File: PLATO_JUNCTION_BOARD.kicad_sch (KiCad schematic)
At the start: 28 parts, among them J1 DE9_Receptacle_MountingHoles, J2 TFM-108-02-L-D, J3 TFM-108-02-L-D, U1 R-78E5.0-0.5

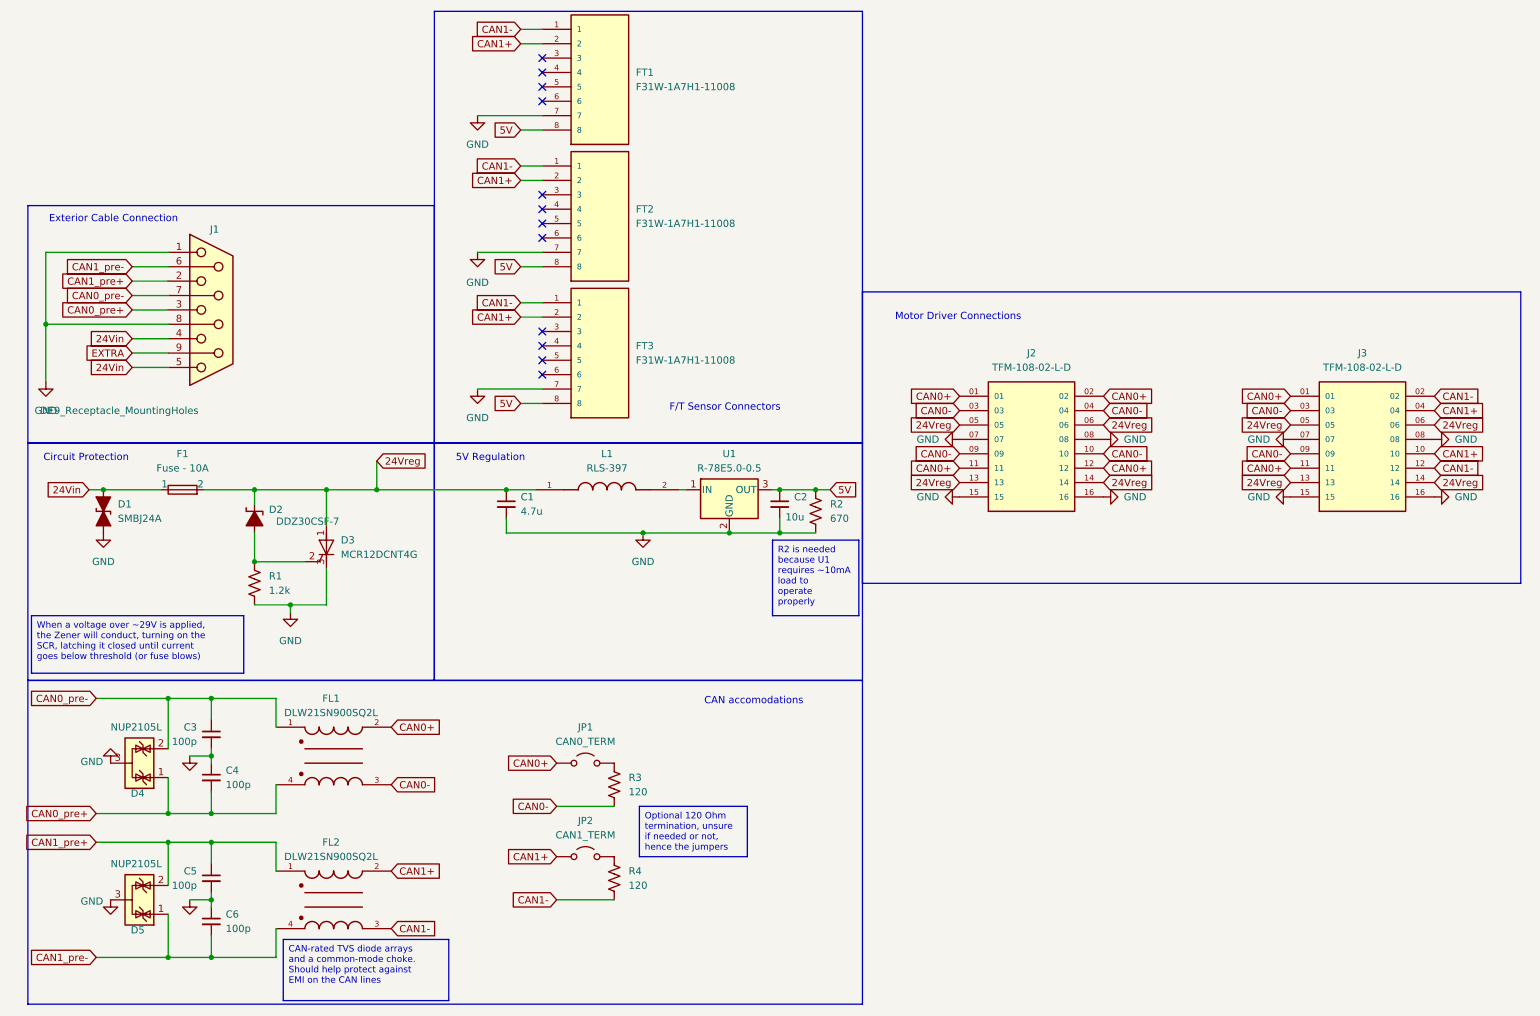
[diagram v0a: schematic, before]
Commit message: Removed choke, added new connector
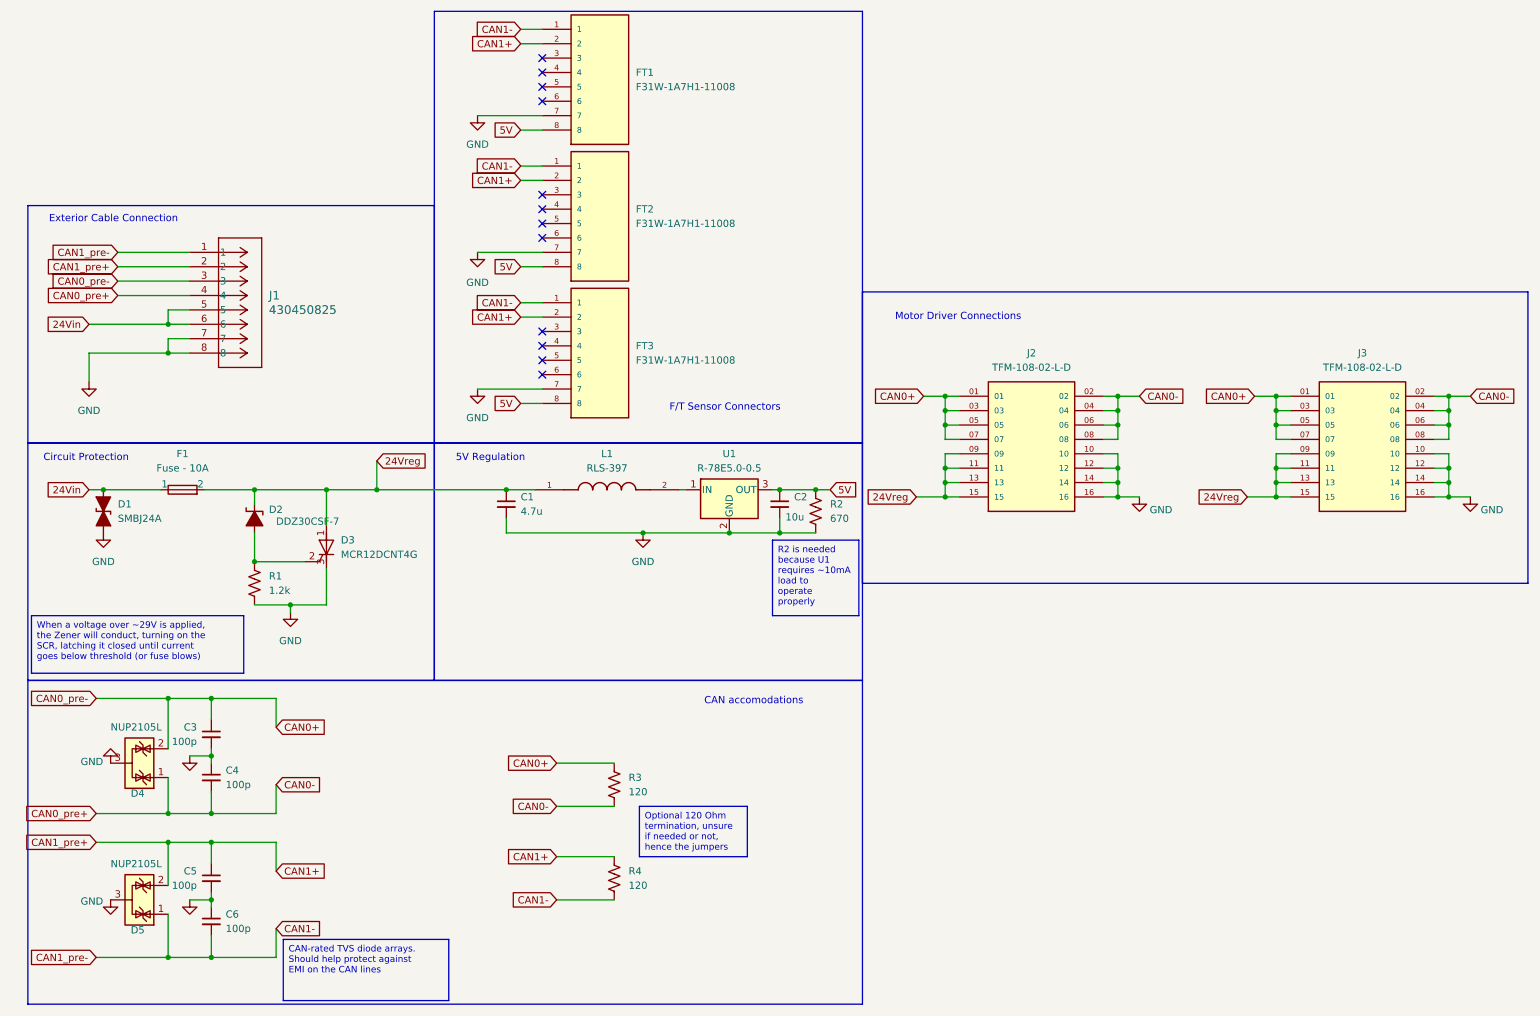
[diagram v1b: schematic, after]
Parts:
- removed FL1, FL2: DLW21SN900SQ2L, DLW21SN900SQ2L:DLW21SN900SQ2L, symbol DLW21SN900SQ2L:DLW21SN900SQ2L
- removed J1: DE9_Receptacle_MountingHoles, Connector_Dsub:DSUB-9_Female_Horizontal_P2.77x2.54mm_EdgePinOffset9.40mm, symbol Connector:DE9_Receptacle
- removed JP1: CAN0_TERM, JumperVariant:SolderJumper-2_P1.3mm_Open_Pad1.0x1.5mm_SMALLER, symbol Jumper:Jumper_2_Open
- removed JP2: CAN1_TERM, JumperVariant:SolderJumper-2_P1.3mm_Open_Pad1.0x1.5mm_SMALLER, symbol Jumper:Jumper_2_Open
- added J1: 430450825, 0430450825:0430450825, symbol 0430450825:430450825
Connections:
- net CAN0_pre+ is gone; now on net CAN0-: C4.2, D4.1 (K)
- net CAN0_pre- is gone; now on net CAN0+: C3.1, D4.2 (K)
- net CAN1_pre+ is gone; now on net CAN1+: C5.1, D5.2 (K)
- net CAN1_pre- is gone; now on net CAN1-: C6.2, D5.1 (K)
- net 24Vin: now also J1.5, J1.6
- net 24Vreg: now also J2.09, J2.11, J2.15, J3.09, J3.11, J3.15; no longer J2.05, J2.06, J2.14, J3.05, J3.06, J3.14
- net CAN0+: now also J2.03, J2.05, J2.07, J3.03, J3.05, J3.07, R3.1, J1.3; no longer J2.02, J2.11, J2.12, J3.11
- net CAN0-: now also J2.02, J2.06, J2.08, J3.02, J3.04, J3.06, J3.08, J1.4; no longer J2.03, J2.09, J2.10, J3.03, J3.09
- net CAN1+: now also R4.1, J1.2; no longer J3.04, J3.10
- net CAN1-: now also J1.1; no longer J3.02, J3.12
- net GND: now also J2.10, J2.12, J2.14, J3.10, J3.12, J3.14, J1.7, J1.8; no longer J2.07, J2.08, J2.15, J3.07, J3.08, J3.15

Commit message: moved 24V and GND pins on J1, changed GND pads to square shapes
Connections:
- net 24Vin: now also J1.7; no longer J1.5
- net GND: now also J1.10, J1.5, J1.9; no longer J1.7
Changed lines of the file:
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@@
 	)
 	(junction
-		(at 102.87 106.68)
+		(at 21.59 82.55)
 		(diameter 0)
 		(color 0 0 0 0)
 	)
 	(junction
-		(at 43.18 82.55)
+		(at 102.87 106.68)
 		(diameter 0)
 		(color 0 0 0 0)
@@
 	)
 	(junction
-		(at 43.18 77.47)
-		(diameter 0)
-		(color 0 0 0 0)
-	)
-	(junction
 		(at 210.82 92.71)
 		(diameter 0)
@@
 	)
 	(junction
+		(at 45.72 77.47)
+		(diameter 0)
+		(color 0 0 0 0)
+	)
+	(junction
 		(at 238.76 95.25)
 		(diameter 0)
@@
 	(wire
 		(pts
-			(xy 29.21 77.47) (xy 43.18 77.47)
-		)
-		(stroke
-			(width 0)
-			(type default)
-		)
-	)
-	(wire
-		(pts
 			(xy 102.87 114.3) (xy 127 114.3)
 		)
@@
 	(wire
 		(pts
+			(xy 45.72 77.47) (xy 45.72 80.01)
+		)
+		(stroke
+			(width 0)
+			(type default)
+		)
+	)
+	(wire
+		(pts
 			(xy 97.79 40.64) (xy 109.22 40.64)
 		)
@@
 	(wire
 		(pts
+			(xy 62.23 59.69) (xy 55.88 59.69)
+		)
+		(stroke
+			(width 0)
+			(type default)
+		)
+	)
+	(wire
+		(pts
 			(xy 273.05 107.95) (xy 269.24 107.95)
 		)
@@
 	(wire
 		(pts
-			(xy 43.18 80.01) (xy 46.99 80.01)
-		)
-		(stroke
-			(width 0)
-			(type default)
-		)
-	)
-	(wire
-		(pts
 			(xy 273.05 90.17) (xy 269.24 90.17)
 		)
@@
 	(wire
 		(pts
-			(xy 29.21 82.55) (xy 43.18 82.55)
-		)
-		(stroke
-			(width 0)
-			(type default)
-		)
-	)
-	(wire
-		(pts
 			(xy 238.76 102.87) (xy 241.3 102.87)
 		)
@@
 	(wire
 		(pts
-			(xy 43.18 77.47) (xy 43.18 74.93)
-		)
-		(stroke
-			(width 0)
-			(type default)
-		)
-	)
-	(wire
-		(pts
 			(xy 214.63 90.17) (xy 210.82 90.17)
 		)
@@
 	(wire
 		(pts
-			(xy 43.18 74.93) (xy 46.99 74.93)
-		)
-		(stroke
-			(width 0)
-			(type default)
-		)
-	)
-	(wire
-		(pts
 			(xy 105.41 43.18) (xy 109.22 43.18)
 		)
@@
 	(wire
 		(pts
-			(xy 43.18 77.47) (xy 46.99 77.47)
-		)
-		(stroke
-			(width 0)
-			(type default)
-		)
-	)
-	(wire
-		(pts
 			(xy 43.18 189.23) (xy 50.8 189.23)
 		)
@@
 	(wire
 		(pts
-			(xy 43.18 82.55) (xy 46.99 82.55)
+			(xy 105.41 52.07) (xy 109.22 52.07)
 		)
 		(stroke
@@
 	(wire
 		(pts
-			(xy 105.41 52.07) (xy 109.22 52.07)
+			(xy 45.72 80.01) (xy 46.99 80.01)
 		)
 		(stroke
@@
 	(wire
 		(pts
-			(xy 29.21 82.55) (xy 29.21 87.63)
+			(xy 21.59 82.55) (xy 21.59 83.82)
 		)
 		(stroke
@@
 	(wire
 		(pts
+			(xy 46.99 74.93) (xy 21.59 74.93)
+		)
+		(stroke
+			(width 0)
+			(type default)
+		)
+	)
+	(wire
+		(pts
 			(xy 50.8 160.02) (xy 50.8 163.83)
 		)
@@
 	(wire
 		(pts
+			(xy 34.29 77.47) (xy 45.72 77.47)
+		)
+		(stroke
+			(width 0)
+			(type default)
+		)
+	)
+	(wire
+		(pts
 			(xy 176.53 90.17) (xy 180.34 90.17)
 		)
@@
 	(wire
 		(pts
-			(xy 43.18 80.01) (xy 43.18 82.55)
+			(xy 21.59 74.93) (xy 21.59 82.55)
 		)
 		(stroke
@@
 	(wire
 		(pts
+			(xy 45.72 77.47) (xy 46.99 77.47)
+		)
+		(stroke
+			(width 0)
+			(type default)
+		)
+	)
+	(wire
+		(pts
 			(xy 157.48 106.68) (xy 160.02 106.68)
 		)
@@
 	(wire
 		(pts
+			(xy 21.59 82.55) (xy 46.99 82.55)
+		)
+		(stroke
+			(width 0)
+			(type default)
+		)
+	)
+	(wire
+		(pts
 			(xy 43.18 168.91) (xy 43.18 176.53)
 		)
@@
 	(global_label "24Vin"
 		(shape input)
-		(at 29.21 77.47 180)
+		(at 34.29 77.47 180)
 		(fields_autoplaced yes)
 		(effects
@@
 		)
 		(property "Intersheetrefs" "${INTERSHEET_REFS}"
-			(at 20.9634 77.47 0)
+			(at 26.0434 77.47 0)
 			(effects
 				(font
@@
 		(pin "4"
 		)
+		(pin "9"
+		)
+		(pin "10"
+		)
 		(instances
 			(project ""
@@
 	)
 	(symbol
+		(lib_id "power:GND")
+		(at 62.23 59.69 0)
+		(mirror y)
+		(unit 1)
+		(exclude_from_sim no)
+		(in_bom yes)
+		(on_board yes)
+		(dnp no)
+		(fields_autoplaced yes)
+		(property "Reference" "#PWR10"
+			(at 62.23 66.04 0)
+			(effects
+				(font
+					(size 1.27 1.27)
+				)
+				(hide yes)
+			)
+		)
+		(property "Value" "GND"
+			(at 62.2301 63.5 90)
+			(effects
+				(font
+					(size 1.27 1.27)
+				)
+				(justify right)
+				(hide yes)
+			)
+		)
+		(property "Footprint" ""
+			(at 62.23 59.69 0)
+			(effects
+				(font
+					(size 1.27 1.27)
+				)
+				(hide yes)
+			)
+		)
+		(property "Datasheet" ""
+			(at 62.23 59.69 0)
+			(effects
+				(font
+					(size 1.27 1.27)
+				)
+				(hide yes)
+			)
+		)
+		(property "Description" "Power symbol creates a global label with name \"GND\" , ground"
+			(at 62.23 59.69 0)
+			(effects
+				(font
+					(size 1.27 1.27)
+				)
+				(hide yes)
+			)
+		)
+		(pin "1"
+		)
+		(instances
+			(project "PLATO_JUNCTION_BOARD"
+				(path "/b029bc8a-eb1a-4550-a6f9-ce3f11ff00d6"
+					(reference "#PWR10")
+					(unit 1)
+				)
+			)
+		)
+	)
+	(symbol
+		(lib_id "power:GND")
+		(at 55.88 87.63 0)
+		(mirror y)
+		(unit 1)
+		(exclude_from_sim no)
+		(in_bom yes)
+		(on_board yes)
+		(dnp no)
+		(fields_autoplaced yes)
+		(property "Reference" "#PWR9"
+			(at 55.88 93.98 0)
+			(effects
+				(font
+					(size 1.27 1.27)
+				)
+				(hide yes)
+			)
+		)
+		(property "Value" "GND"
+			(at 55.88 92.71 0)
+			(effects
+				(font
+					(size 1.27 1.27)
+				)
+				(hide yes)
+			)
+		)
+		(property "Footprint" ""
+			(at 55.88 87.63 0)
+			(effects
+				(font
+					(size 1.27 1.27)
+				)
+				(hide yes)
+			)
+		)
+		(property "Datasheet" ""
+			(at 55.88 87.63 0)
+			(effects
+				(font
+					(size 1.27 1.27)
+				)
+				(hide yes)
+			)
+		)
+		(property "Description" "Power symbol creates a global label with name \"GND\" , ground"
+			(at 55.88 87.63 0)
+			(effects
+				(font
+					(size 1.27 1.27)
+				)
+				(hide yes)
+			)
+		)
+		(pin "1"
+		)
+		(instances
+			(project "PLATO_JUNCTION_BOARD"
+				(path "/b029bc8a-eb1a-4550-a6f9-ce3f11ff00d6"
+					(reference "#PWR9")
+					(unit 1)
+				)
+			)
+		)
+	)
+	(symbol
 		(lib_id "RLS-397:RLS-397")
 		(at 120.65 106.68 0)
@@
 	(symbol
 		(lib_id "power:GND")
-		(at 29.21 87.63 0)
+		(at 21.59 83.82 0)
 		(mirror y)
 		(unit 1)
@@
 		(fields_autoplaced yes)
 		(property "Reference" "#PWR01"
-			(at 29.21 93.98 0)
+			(at 21.59 90.17 0)
 			(effects
 				(font
@@
 		)
 		(property "Value" "GND"
-			(at 29.21 92.71 0)
+			(at 21.59 88.9 0)
 			(effects
 				(font
@@
 		)
 		(property "Footprint" ""
-			(at 29.21 87.63 0)
+			(at 21.59 83.82 0)
 			(effects
 				(font
@@
 		)
 		(property "Datasheet" ""
-			(at 29.21 87.63 0)
+			(at 21.59 83.82 0)
 			(effects
 				(font
@@
 		)
 		(property "Description" "Power symbol creates a global label with name \"GND\" , ground"
-			(at 29.21 87.63 0)
+			(at 21.59 83.82 0)
 			(effects
 				(font

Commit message: added oshpark drc
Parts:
- C1: Digikey https://www.digikey.com/short/t0qqff27 -> owned
- C2: Digikey https://www.digikey.com/short/z7bhhmmm -> owned
- D1: Digikey https://www.digikey.com/short/t83n8jjn -> owned
- D2: Digikey https://www.digikey.com/short/2d2238z9 -> owned
- D3: Digikey https://www.digikey.com/short/zm0rcz48 -> owned
- D4, D5: Digikey https://www.digikey.com/short/0hmz210w -> owned
- F1: Digikey https://www.digikey.com/short/f2p10b24 -> owned - buy 20A fuse
- J1: Digikey (none) -> https://www.digikey.com/short/9qj3z9bw
- J2, J3: Digikey https://www.digikey.com/short/qtbd5z2t -> owned, maybe find locking
- R1, R2, R3, R4: Digikey (none) -> owned
- U1: Digikey https://www.digikey.com/short/02m50734 -> owned
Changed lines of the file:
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@@
 			)
 		)
-		(property "Digikey" "https://www.digikey.com/short/2d2238z9"
+		(property "Digikey" "owned"
 			(at 58.42 111.76 0)
 			(effects
@@
 			)
 		)
+		(property "Digikey" "owned"
+			(at 121.92 158.75 0)
+			(effects
+				(font
+					(size 1.27 1.27)
+				)
+				(hide yes)
+			)
+		)
 		(pin "1"
 		)
@@
 			)
 		)
-		(property "Digikey" "https://www.digikey.com/short/qtbd5z2t"
+		(property "Digikey" "owned, maybe find locking"
 			(at 195.58 100.33 0)
 			(effects
@@
 			)
 		)
+		(property "Digikey" "owned"
+			(at 121.92 175.26 0)
+			(effects
+				(font
+					(size 1.27 1.27)
+				)
+				(hide yes)
+			)
+		)
 		(pin "1"
 		)
@@
 			)
 		)
-		(property "Digikey" "https://www.digikey.com/short/0hmz210w"
+		(property "Digikey" "owned"
 			(at 38.1 154.94 0)
 			(effects
@@
 			)
 		)
-		(property "Digikey" "https://www.digikey.com/short/02m50734"
+		(property "Digikey" "owned"
 			(at 142.24 106.68 0)
 			(effects
@@
 			)
 		)
-		(property "Digikey" "https://www.digikey.com/short/t83n8jjn"
+		(property "Digikey" "owned"
 			(at 31.75 110.49 90)
 			(effects
@@
 			)
 		)
+		(property "Digikey" "https://www.digikey.com/short/9qj3z9bw"
+			(at 46.99 64.77 0)
+			(effects
+				(font
+					(size 1.27 1.27)
+				)
+				(hide yes)
+			)
+		)
 		(pin "1"
 		)
@@
 			)
 		)
-		(property "Digikey" "https://www.digikey.com/short/0hmz210w"
+		(property "Digikey" "owned"
 			(at 38.1 179.07 0)
 			(effects
@@
 			)
 		)
-		(property "Digikey" "https://www.digikey.com/short/z7bhhmmm"
+		(property "Digikey" "owned"
 			(at 151.13 109.22 0)
 			(effects
@@
 			)
 		)
-		(property "Digikey" "https://www.digikey.com/short/f2p10b24"
+		(property "Digikey" "owned - buy 20A fuse"
 			(at 45.974 110.998 90)
 			(effects
@@
 		(dnp no)
 		(fields_autoplaced yes)
-		(property "Reference" "#PWR10"
+		(property "Reference" "#PWR010"
 			(at 62.23 66.04 0)
 			(effects
@@
 			(project "PLATO_JUNCTION_BOARD"
 				(path "/b029bc8a-eb1a-4550-a6f9-ce3f11ff00d6"
-					(reference "#PWR10")
+					(reference "#PWR010")
 					(unit 1)
 				)
@@
 		(dnp no)
 		(fields_autoplaced yes)
-		(property "Reference" "#PWR9"
+		(property "Reference" "#PWR09"
 			(at 55.88 93.98 0)
 			(effects
@@
 			(project "PLATO_JUNCTION_BOARD"
 				(path "/b029bc8a-eb1a-4550-a6f9-ce3f11ff00d6"
-					(reference "#PWR9")
+					(reference "#PWR09")
 					(unit 1)
 				)
@@
 			)
 		)
-		(property "Digikey" "https://www.digikey.com/short/t0qqff27"
+		(property "Digikey" "owned"
 			(at 102.87 109.22 0)
 			(effects
@@
 			)
 		)
-		(property "Digikey" "https://www.digikey.com/short/qtbd5z2t"
+		(property "Digikey" "owned, maybe find locking"
 			(at 254 100.33 0)
 			(effects
@@
 			)
 		)
+		(property "Digikey" "owned"
+			(at 58.42 123.19 0)
+			(effects
+				(font
+					(size 1.27 1.27)
+				)
+				(hide yes)
+			)
+		)
 		(pin "1"
 		)
@@
 			)
 		)
-		(property "Digikey" "https://www.digikey.com/short/zm0rcz48"
+		(property "Digikey" "owned"
 			(at 71.12 116.84 0)
 			(effects
@@
 			(at 157.48 110.49 0)
 			(effects
+				(font
+					(size 1.27 1.27)
+				)
+				(hide yes)
+			)
+		)
+		(property "Digikey" "owned"
+			(at 157.48 110.49 0)
+			(effects
